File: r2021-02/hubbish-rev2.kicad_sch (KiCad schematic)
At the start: 4 parts

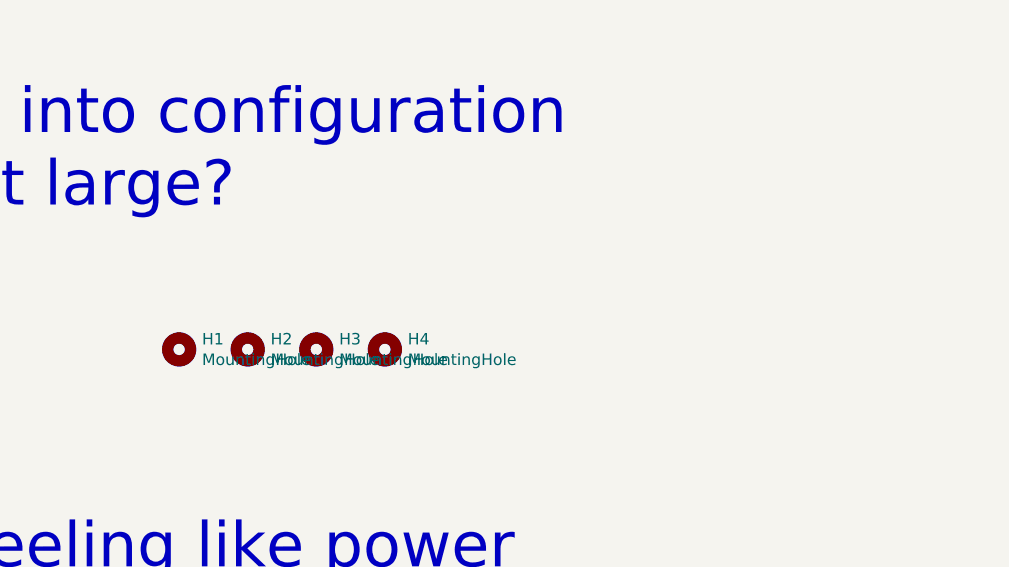
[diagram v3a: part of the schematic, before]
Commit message: sch: rev2: update to latest kicad, add power flags.
cleared all ERC errors/warnings
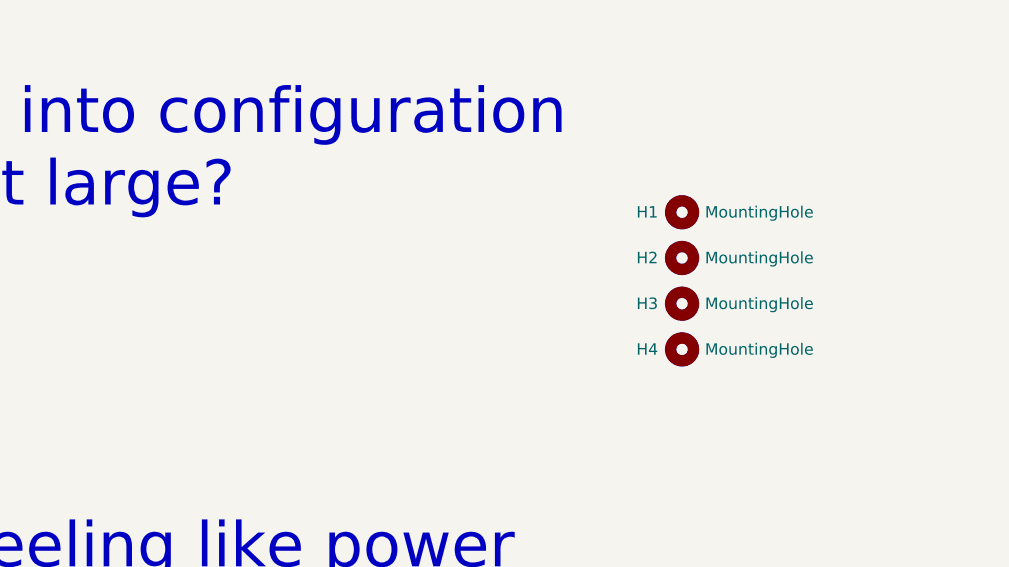
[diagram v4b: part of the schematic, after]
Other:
- moved on the sheet: H1, H2, H3, H4
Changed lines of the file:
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@@
     (effects (font (size 5.0038 5.0038)) (justify left bottom))
   )
-  (symbol (lib_id "Mechanical:MountingHole") (at 177.8 106.68 0) (unit 1)
+  (symbol (lib_id "Mechanical:MountingHole") (at 233.68 91.44 0) (unit 1)
     (in_bom yes) (on_board yes)
-    (property "Reference" "H1" (id 0) (at 180.34 105.537 0)
-      (effects (font (size 1.27 1.27)) (justify left))
-    )
-    (property "Value" "MountingHole" (id 1) (at 180.34 107.823 0)
-      (effects (font (size 1.27 1.27)) (justify left))
-    )
-    (property "Footprint" "MountingHole:MountingHole_2.7mm_M2.5" (id 2) (at 177.8 106.68 0)
-      (effects (font (size 1.27 1.27)) hide)
-    )
-    (property "Datasheet" "~" (id 3) (at 177.8 106.68 0)
-      (effects (font (size 1.27 1.27)) hide)
-    )
-  )
-  (symbol (lib_name "Mechanical:MountingHole_1") (lib_id "Mechanical:MountingHole") (at 185.42 106.68 0) (unit 1)
+    (property "Reference" "H1" (id 0) (at 228.6 91.44 0)
+      (effects (font (size 1.27 1.27)) (justify left))
+    )
+    (property "Value" "MountingHole" (id 1) (at 236.22 91.44 0)
+      (effects (font (size 1.27 1.27)) (justify left))
+    )
+    (property "Footprint" "MountingHole:MountingHole_2.7mm_M2.5" (id 2) (at 233.68 91.44 0)
+      (effects (font (size 1.27 1.27)) hide)
+    )
+    (property "Datasheet" "~" (id 3) (at 233.68 91.44 0)
+      (effects (font (size 1.27 1.27)) hide)
+    )
+  )
+  (symbol (lib_id "Mechanical:MountingHole") (at 233.68 96.52 0) (unit 1)
     (in_bom yes) (on_board yes)
-    (property "Reference" "H2" (id 0) (at 187.96 105.537 0)
-      (effects (font (size 1.27 1.27)) (justify left))
-    )
-    (property "Value" "MountingHole" (id 1) (at 187.96 107.823 0)
-      (effects (font (size 1.27 1.27)) (justify left))
-    )
-    (property "Footprint" "MountingHole:MountingHole_2.7mm_M2.5" (id 2) (at 185.42 106.68 0)
-      (effects (font (size 1.27 1.27)) hide)
-    )
-    (property "Datasheet" "~" (id 3) (at 185.42 106.68 0)
-      (effects (font (size 1.27 1.27)) hide)
-    )
-  )
-  (symbol (lib_name "Mechanical:MountingHole_2") (lib_id "Mechanical:MountingHole") (at 193.04 106.68 0) (unit 1)
+    (property "Reference" "H2" (id 0) (at 228.6 96.52 0)
+      (effects (font (size 1.27 1.27)) (justify left))
+    )
+    (property "Value" "MountingHole" (id 1) (at 236.22 96.52 0)
+      (effects (font (size 1.27 1.27)) (justify left))
+    )
+    (property "Footprint" "MountingHole:MountingHole_2.7mm_M2.5" (id 2) (at 233.68 96.52 0)
+      (effects (font (size 1.27 1.27)) hide)
+    )
+    (property "Datasheet" "~" (id 3) (at 233.68 96.52 0)
+      (effects (font (size 1.27 1.27)) hide)
+    )
+  )
+  (symbol (lib_id "Mechanical:MountingHole") (at 233.68 101.6 0) (unit 1)
     (in_bom yes) (on_board yes)
-    (property "Reference" "H3" (id 0) (at 195.58 105.537 0)
-      (effects (font (size 1.27 1.27)) (justify left))
-    )
-    (property "Value" "MountingHole" (id 1) (at 195.58 107.823 0)
-      (effects (font (size 1.27 1.27)) (justify left))
-    )
-    (property "Footprint" "MountingHole:MountingHole_2.7mm_M2.5" (id 2) (at 193.04 106.68 0)
-      (effects (font (size 1.27 1.27)) hide)
-    )
-    (property "Datasheet" "~" (id 3) (at 193.04 106.68 0)
-      (effects (font (size 1.27 1.27)) hide)
-    )
-  )
-  (symbol (lib_name "Mechanical:MountingHole_3") (lib_id "Mechanical:MountingHole") (at 200.66 106.68 0) (unit 1)
+    (property "Reference" "H3" (id 0) (at 228.6 101.6 0)
+      (effects (font (size 1.27 1.27)) (justify left))
+    )
+    (property "Value" "MountingHole" (id 1) (at 236.22 101.6 0)
+      (effects (font (size 1.27 1.27)) (justify left))
+    )
+    (property "Footprint" "MountingHole:MountingHole_2.7mm_M2.5" (id 2) (at 233.68 101.6 0)
+      (effects (font (size 1.27 1.27)) hide)
+    )
+    (property "Datasheet" "~" (id 3) (at 233.68 101.6 0)
+      (effects (font (size 1.27 1.27)) hide)
+    )
+  )
+  (symbol (lib_id "Mechanical:MountingHole") (at 233.68 106.68 0) (unit 1)
     (in_bom yes) (on_board yes)
-    (property "Reference" "H4" (id 0) (at 203.2 105.537 0)
-      (effects (font (size 1.27 1.27)) (justify left))
-    )
-    (property "Value" "MountingHole" (id 1) (at 203.2 107.823 0)
-      (effects (font (size 1.27 1.27)) (justify left))
-    )
-    (property "Footprint" "MountingHole:MountingHole_2.7mm_M2.5" (id 2) (at 200.66 106.68 0)
-      (effects (font (size 1.27 1.27)) hide)
-    )
-    (property "Datasheet" "~" (id 3) (at 200.66 106.68 0)
+    (property "Reference" "H4" (id 0) (at 228.6 106.68 0)
+      (effects (font (size 1.27 1.27)) (justify left))
+    )
+    (property "Value" "MountingHole" (id 1) (at 236.22 106.68 0)
+      (effects (font (size 1.27 1.27)) (justify left))
+    )
+    (property "Footprint" "MountingHole:MountingHole_2.7mm_M2.5" (id 2) (at 233.68 106.68 0)
+      (effects (font (size 1.27 1.27)) hide)
+    )
+    (property "Datasheet" "~" (id 3) (at 233.68 106.68 0)
       (effects (font (size 1.27 1.27)) hide)
     )
@@
       (reference "H4") (unit 1) (value "MountingHole") (footprint "MountingHole:MountingHole_2.7mm_M2.5")
     )
+    (path "/00000000-0000-0000-0000-00005e1ad3c1/03a04717-76b8-4a9f-af44-8692a789da18"
+      (reference "#FLG0101") (unit 1) (value "PWR_FLAG") (footprint "")
+    )
+    (path "/00000000-0000-0000-0000-00005e1ad3c1/dffc50c6-02f5-4825-bf9e-485da983375d"
+      (reference "#FLG0102") (unit 1) (value "PWR_FLAG") (footprint "")
+    )
+    (path "/00000000-0000-0000-0000-00005e1ad3c1/9057f5dd-c0ae-40d7-942c-03230b289e23"
+      (reference "#FLG0103") (unit 1) (value "PWR_FLAG") (footprint "")
+    )
     (path "/00000000-0000-0000-0000-00005e1ad3c1/00000000-0000-0000-0000-00005e1ae764"
       (reference "#PWR01") (unit 1) (value "+5V") (footprint "")
@@
       (reference "#PWR0111") (unit 1) (value "GND") (footprint "")
     )
+    (path "/00000000-0000-0000-0000-00005e1ad3c1/f39521b1-f0ac-4c80-b4a5-690a746901cc"
+      (reference "#PWR0112") (unit 1) (value "GND") (footprint "")
+    )
     (path "/00000000-0000-0000-0000-00005e1ad3c1/2afd0e91-f8ed-4dd0-aec7-409dbb69b8f6"
       (reference "#PWR0113") (unit 1) (value "GND") (footprint "")
     )
-    (path "/00000000-0000-0000-0000-00005e1ad3c1/f39521b1-f0ac-4c80-b4a5-690a746901cc"
-      (reference "#PWR?") (unit 1) (value "GND") (footprint "")
+    (path "/00000000-0000-0000-0000-00005e1ad3c1/b93a42ca-8edf-4807-b214-9335c9b4fdf1"
+      (reference "#PWR0118") (unit 1) (value "GNDPWR") (footprint "")
     )
     (path "/00000000-0000-0000-0000-00005e1ad3c1/00000000-0000-0000-0000-00005e1e3858"
@@
     )
     (path "/00000000-0000-0000-0000-00005e1ad3c1/89b7d82d-9da4-47f3-8e7e-1e17524d66a6"
-      (reference "D?") (unit 1) (value "6.8V Zener or so") (footprint "Diode_SMD:D_SOD-923")
+      (reference "D13") (unit 1) (value "6.8V Zener or so") (footprint "Diode_SMD:D_SOD-123F")
     )
     (path "/00000000-0000-0000-0000-00005e1ad3c1/00000000-0000-0000-0000-00005e82db4d"
@@
     )
     (path "/00000000-0000-0000-0000-00005e1ad3c1/b2cc5568-ec48-4a3a-8148-0633d4f4436c"
-      (reference "Q?") (unit 1) (value "Si4435") (footprint "Package_SO:SOIC-8_3.9x4.9mm_P1.27mm")
+      (reference "Q1") (unit 1) (value "Si4435") (footprint "Package_SO:SOIC-8_3.9x4.9mm_P1.27mm")
     )
     (path "/00000000-0000-0000-0000-00005e1ad3c1/00000000-0000-0000-0000-00005e1aec53"
@@
     )
     (path "/00000000-0000-0000-0000-00005e1ad3c1/8ab8ffe1-dcc0-4402-9a12-5a5bf1a58fc6"
-      (reference "R?") (unit 1) (value "330") (footprint "")
+      (reference "R26") (unit 1) (value "330") (footprint "Resistor_SMD:R_0603_1608Metric")
     )
     (path "/00000000-0000-0000-0000-00005e1ad3c1/00000000-0000-0000-0000-00005e1aeac8"
@@
       (reference "#PWR048") (unit 1) (value "GND") (footprint "")
     )
-    (path "/00000000-0000-0000-0000-00005e1ad41f/00000000-0000-0000-0000-00005e20d47d"
-      (reference "#PWR049") (unit 1) (value "+5V") (footprint "")
-    )
     (path "/00000000-0000-0000-0000-00005e1ad41f/00000000-0000-0000-0000-00005e20d4b6"
       (reference "#PWR050") (unit 1) (value "GND") (footprint "")
@@
       (reference "#PWR0116") (unit 1) (value "GND") (footprint "")
     )
+    (path "/00000000-0000-0000-0000-00005e1ad41f/a01ba239-fdb5-4c3a-bd75-f77847924dc5"
+      (reference "#PWR0117") (unit 1) (value "+5V") (footprint "")
+    )
     (path "/00000000-0000-0000-0000-00005e1ad41f/9d15285e-cd1f-4073-9cef-1e97740ce537"

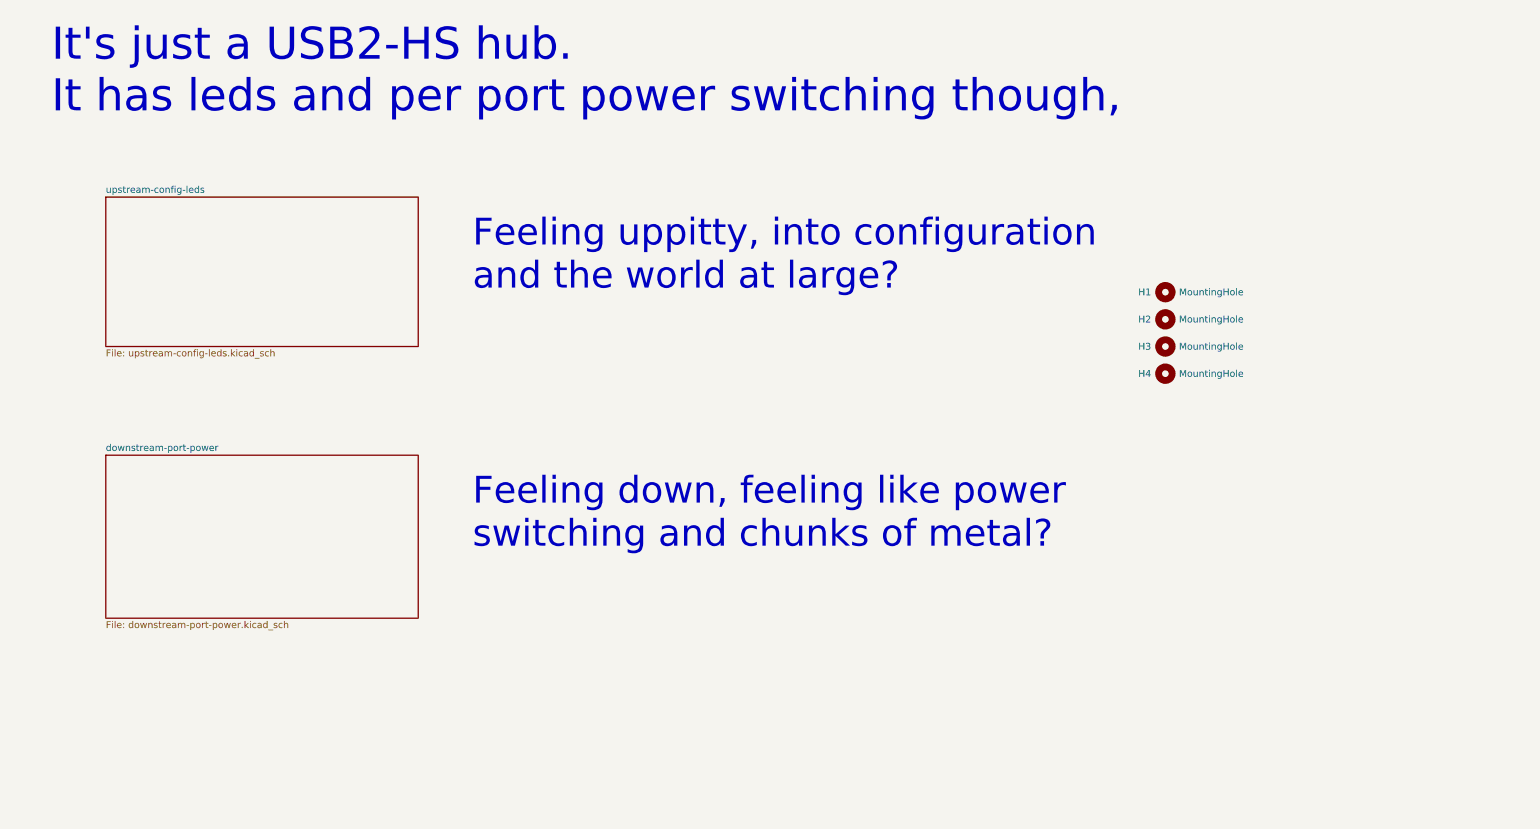
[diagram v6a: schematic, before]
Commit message: hw-rev2: break out power input to a new sheet
It was always a bit crowded there, and now that we need to pick new
parts, we want a little more space...
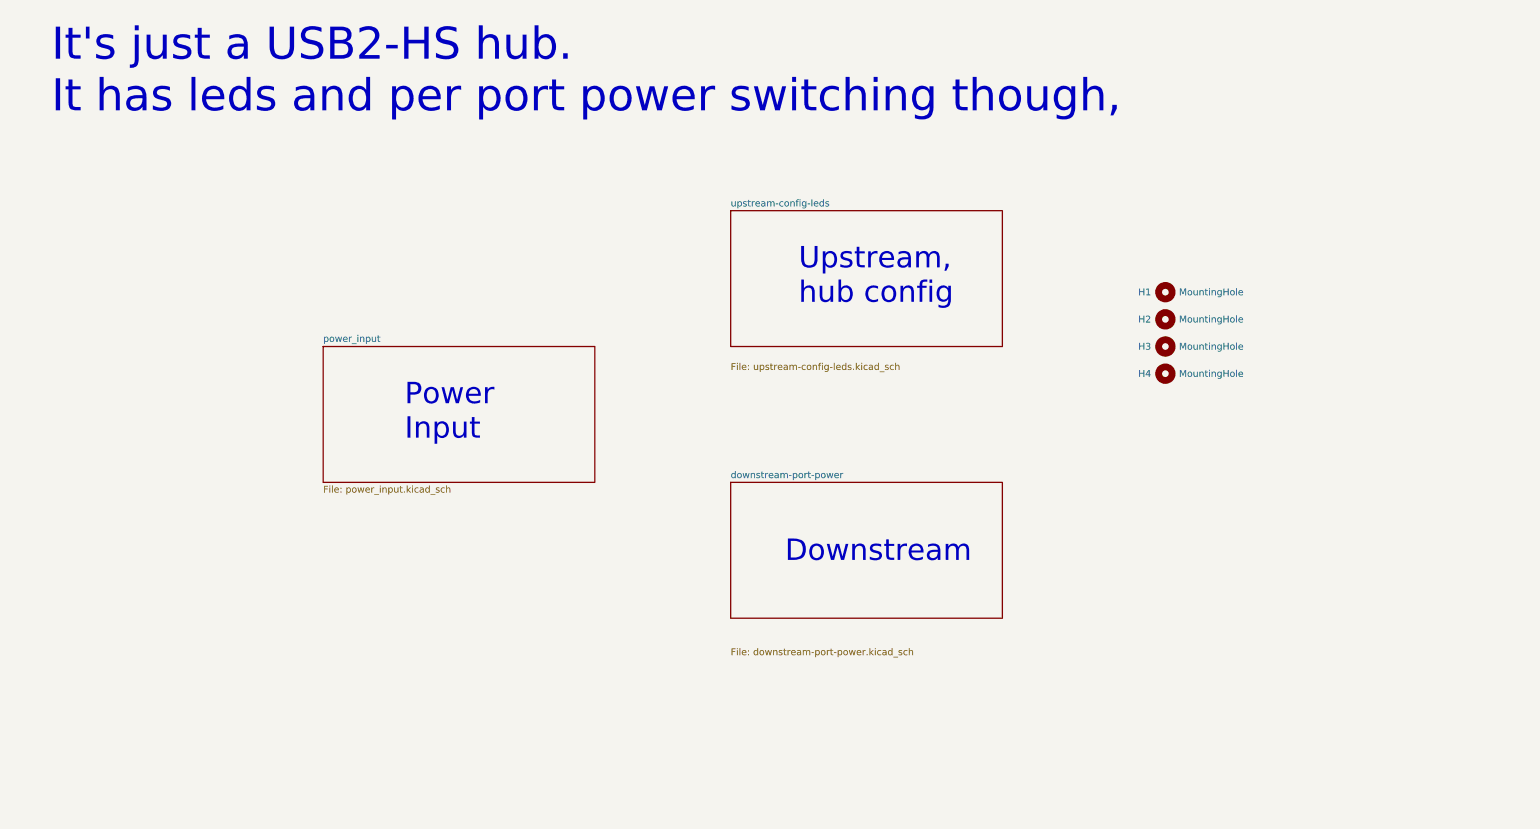
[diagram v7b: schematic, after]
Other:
- added sheet power_input (power_input.kicad_sch)
- note added: "Downstream"
- note added: "Power Input"
- note added: "Upstream, hub config"
- note removed: "Feeling down, feeling like power switching and chunks of metal?"
- note removed: "Feeling uppitty, into configuration and the world at large?"
